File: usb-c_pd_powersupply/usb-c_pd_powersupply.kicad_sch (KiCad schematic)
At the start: 29 parts

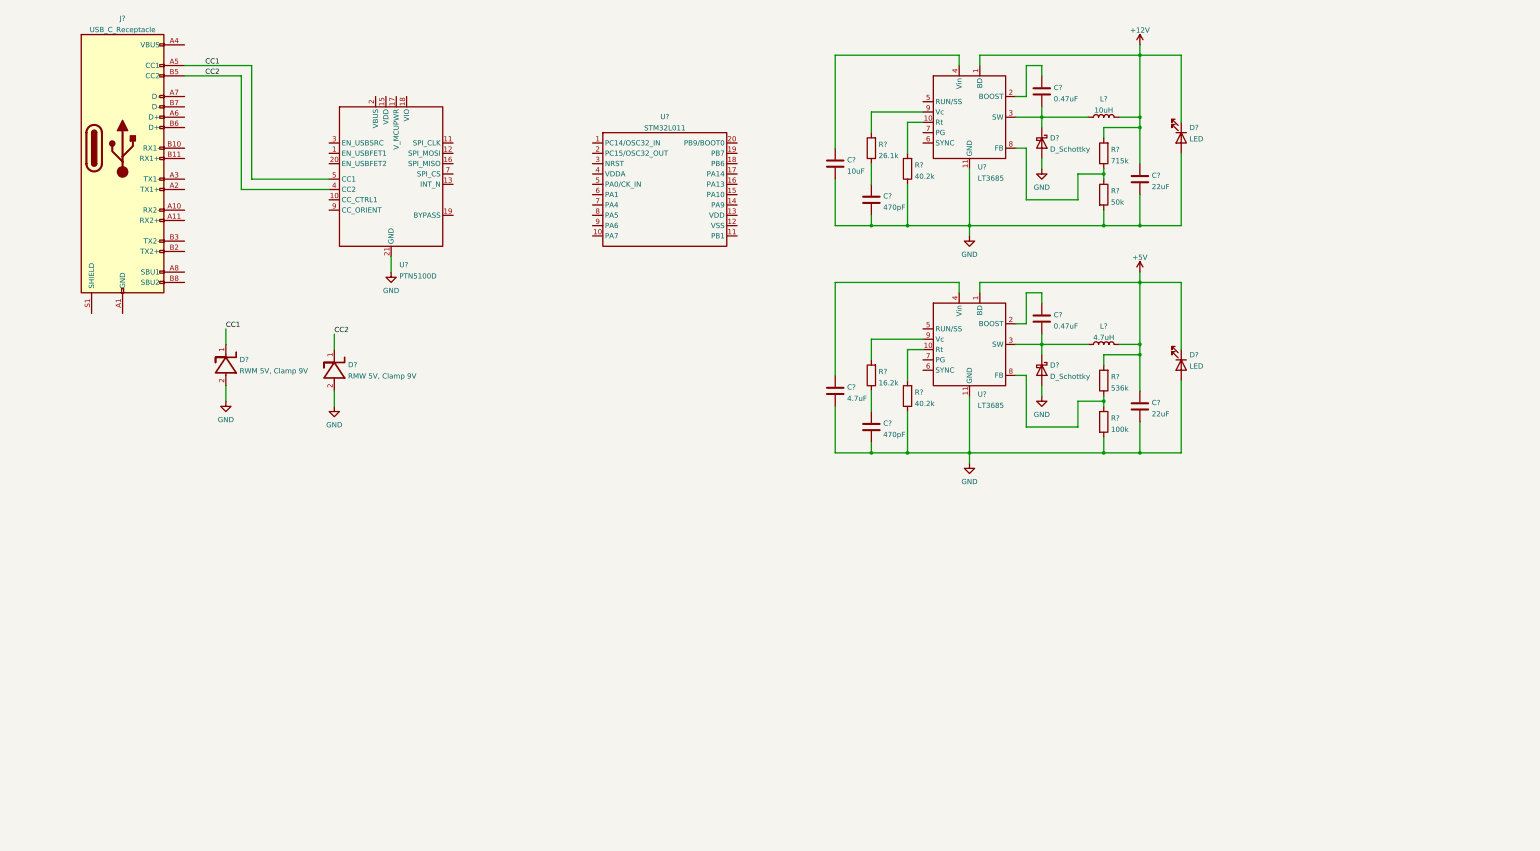
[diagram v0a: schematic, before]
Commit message: WIP on USB-C power supply
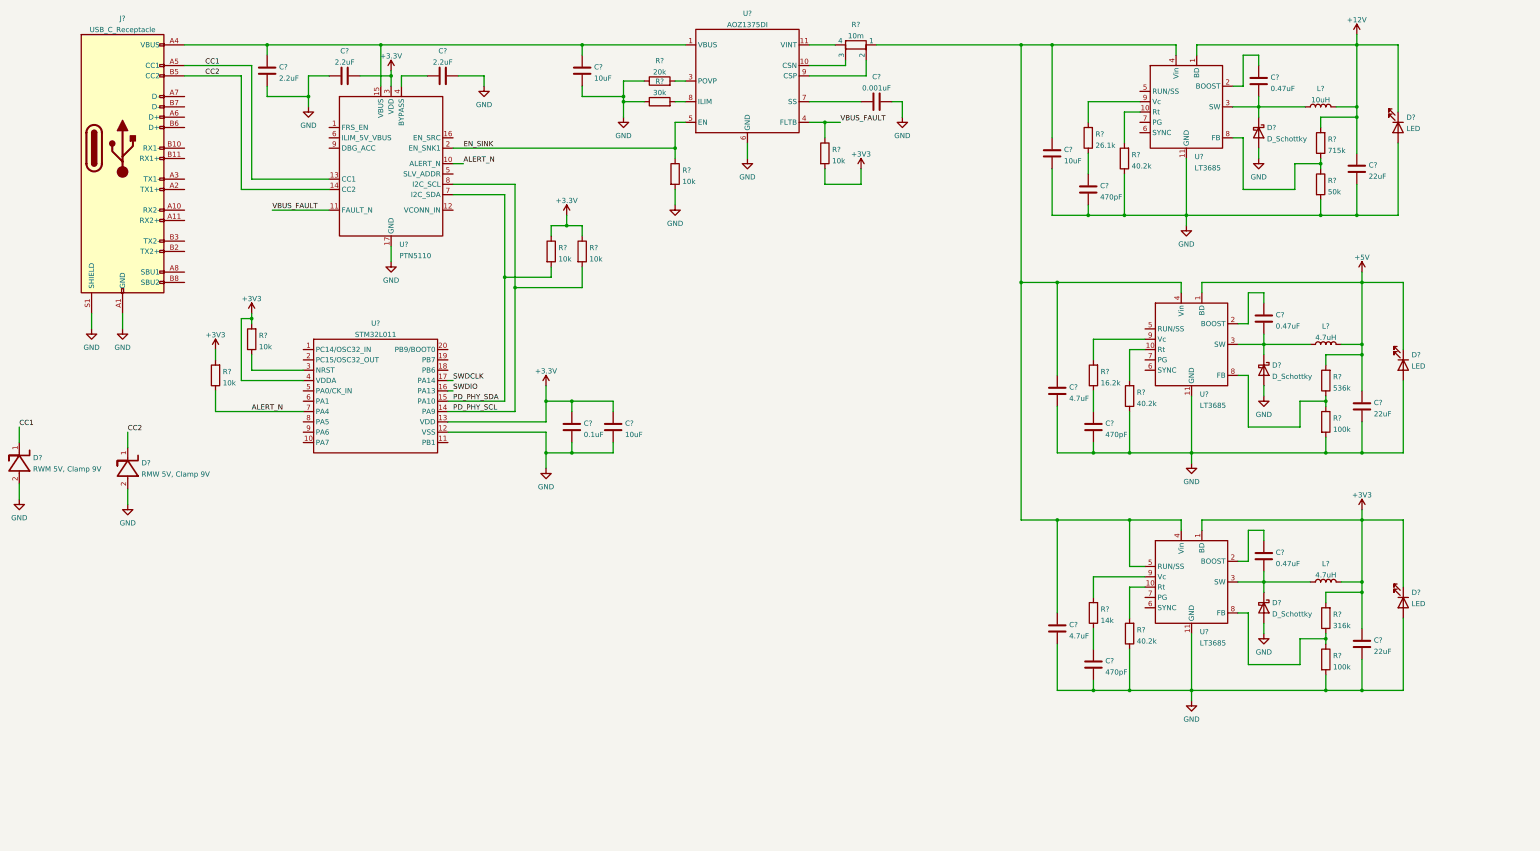
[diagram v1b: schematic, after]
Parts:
- removed U?: PTN5100D, Custom:HVQFN-20, symbol Custom:PTN5100D
- added C? (x2): 10uF, symbol Device:C
- added C?: 0.001uF, symbol Device:C
- added C?: 0.47uF, symbol Device:C
- added C?: 4.7uF, symbol Device:C
- added C?: 470pF, symbol Device:C
- added C? (x3): 2.2uF, symbol Device:C
- added C?: 22uF, symbol Device:C
- added C?: 0.1uF, symbol Device:C
- added D?: LED, symbol Device:LED
- added D?: D_Schottky, symbol Device:D_Schottky
- added L?: 4.7uH, symbol Device:L
- added R? (x6): 10k, symbol Device:R
- added R?: 10m, symbol Device:R_Shunt
- added R?: 14k, symbol Device:R
- added R?: 20k, symbol Device:R
- added R?: 30k, symbol Device:R
- added R?: 100k, symbol Device:R
- added R?: 316k, symbol Device:R
- added R?: 40.2k, symbol Device:R
- added U?: LT3685, Custom:DFN-10, symbol Custom:LT3685
- added U?: PTN5110, Custom:HX2QFN16, symbol Custom:PTN5110
- added U?: AOZ1375DI, Custom:DFN-12L, symbol Custom:AOZ1375DI
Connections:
- net CC1: now also U?.13 (CC1)
- net CC2: now also U?.14 (CC2)
- net GND: now also J?.A1 (GND), J?.A12 (GND), J?.B1 (GND), J?.B12 (GND), J?.S1 (SHIELD), U?.12 (VSS), C?.1, C?.1, C?.2, C?.2, C?.2, C?.2, C?.2, C?.2, C?.2, C?.2, D?.2 (A), D?.2 (A), R?.1, R?.1, R?.1, R?.2, R?.2, U?.11 (GND), U?.13 (GND), U?.17 (GND), U?.6 (GND)
- net at C?.1, U?.4 (Vin): now also C?.1, U?.4 (Vin), C?.1, R?.1, U?.4 (Vin), U?.5 (RUN/SS)
- net at J?.A4 (VBUS), J?.A9 (VBUS), J?.B4 (VBUS)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: now also C?.1, C?.2, U?.1 (VBUS), U?.15 (VBUS)
- net +3V3: now reaches U?.13 (VDD)
- net +3V3: now also U?.4 (VDDA), C?.1, C?.1, C?.1, C?.2, D?.1 (K), L?.2, R?.1, R?.1, R?.2, R?.2, R?.2, R?.2, U?.1 (BD), U?.3 (VDD)
- net PD_PHY_SCL: now reaches U?.14 (PA9)
- net PD_PHY_SCL: now also R?.2, U?.8 (I2C_SCL)
- net PD_PHY_SDA: now reaches U?.15 (PA10)
- net PD_PHY_SDA: now also R?.2, U?.7 (I2C_SDA)
- net SWDIO: now reaches U?.16 (PA13)
- net SWDCLK: now reaches U?.17 (PA14)
- net at U?.3 (NRST): now also R?.1
- net ALERT_N: now reaches U?.7 (PA4)
- net ALERT_N: now also R?.1, U?.10 (ALERT_N)
- new net: C?.1, U?.7 (SS)
- new net: C?.1, U?.2 (BOOST)
- new net: C?.2, D?.1 (K), L?.1, U?.3 (SW)
- new net: C?.1, R?.1
- new net: R?.2, U?.9 (CSP)
- new net: R?.3, U?.10 (CSN)
- new net: R?.4, U?.11 (VINT)
- new net: R?.2, U?.9 (Vc)
- new net: R?.2, U?.10 (Rt)
- new net: R?.1, R?.1, U?.8 (FB)
- new net: C?.1, U?.4 (BYPASS)
- new net: R?.2, U?.3 (POVP)
- new net: R?.2, U?.8 (ILIM)
- new net EN_SINK: R?.1, U?.2 (EN_SNK1), U?.5 (EN)
- new net VBUS_FAULT: R?.1, U?.11 (FAULT_N), U?.4 (FLTB)
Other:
- moved on the sheet: C?, D?, L?, R?, U?

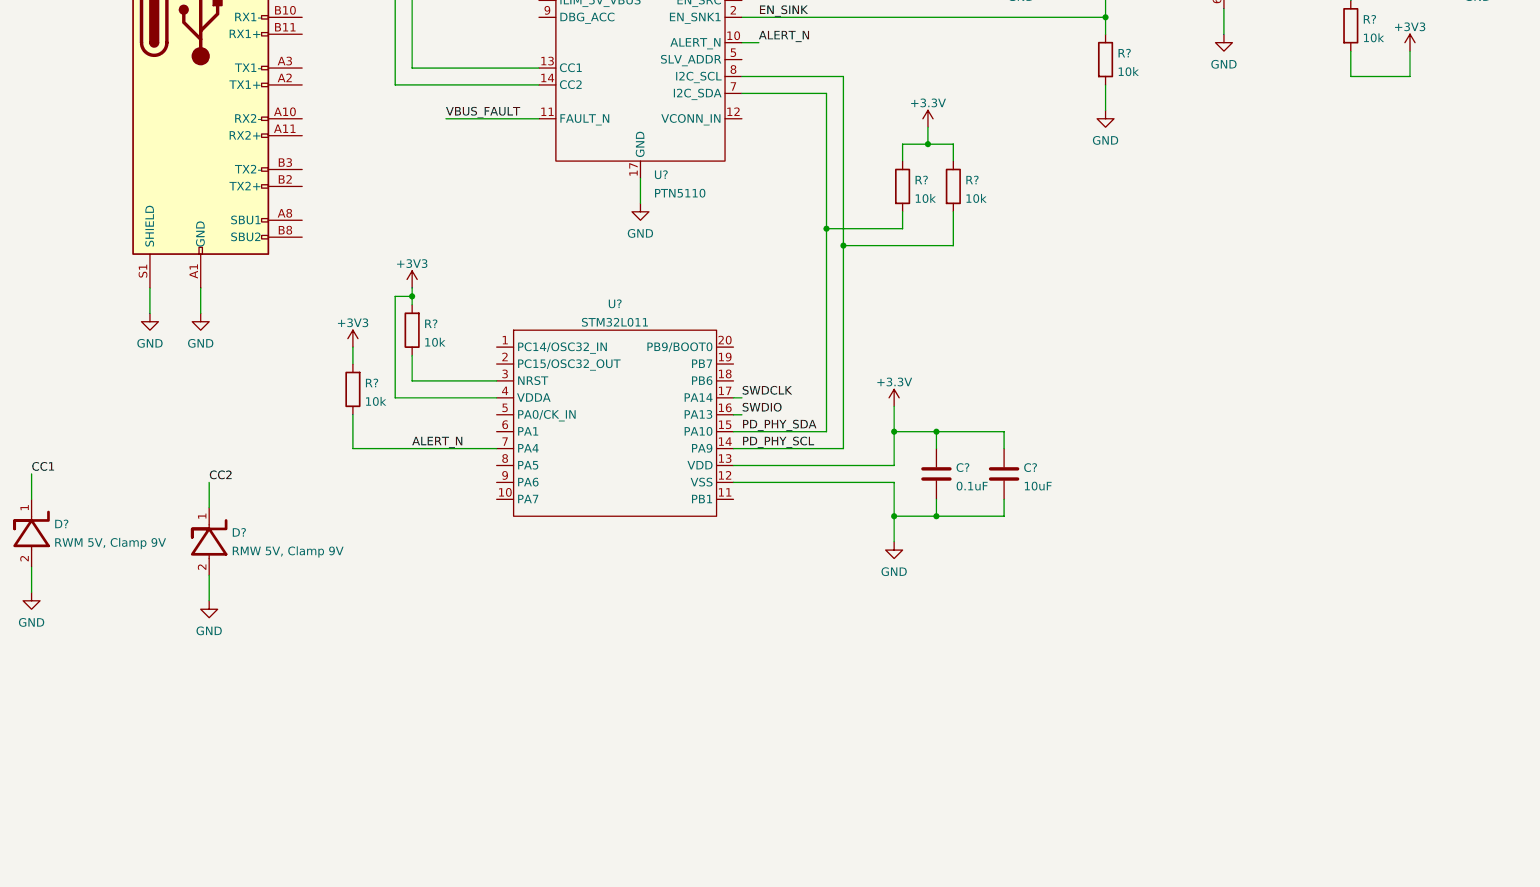
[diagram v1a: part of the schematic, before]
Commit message: Schematic first pass for pd supply
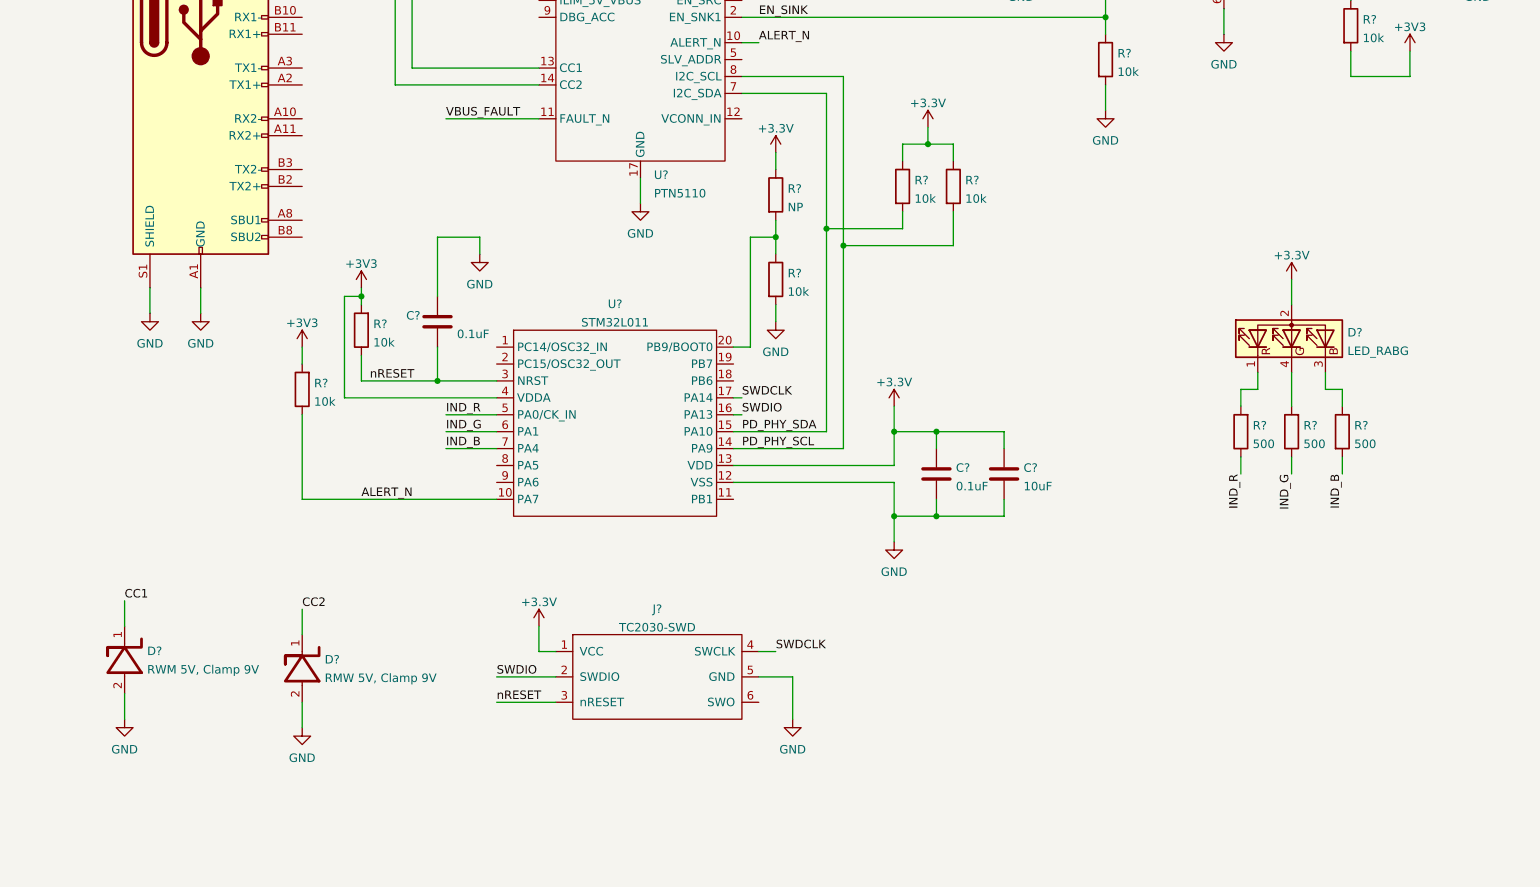
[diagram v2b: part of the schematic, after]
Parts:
- added C?: 0.1uF, symbol Device:C
- added D?: LED_RABG, symbol Device:LED_RABG
- added J?: TC2030-SWD, Custom:TC2030-IDC-FP, symbol Custom:TC2030-SWD
- added R? (x3): 500, symbol Device:R
- added R?: NP, symbol Device:R
- added R?: 10k, symbol Device:R
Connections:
- net +3V3: now also D?.2 (A), J?.1 (VCC), R?.1
- net ALERT_N: now also U?.10 (PA7); no longer U?.7 (PA4)
- net GND: now also C?.1, J?.5 (GND), R?.2
- net SWDCLK: now also J?.4 (SWCLK)
- net SWDIO: now also J?.2 (SWDIO)
- net nRESET: now reaches R?.1, U?.3 (NRST)
- net nRESET: now also C?.2, J?.3 (nRESET)
- net at U?.20 (PB9/BOOT0): now also R?.1, R?.2
- net IND_R: now reaches U?.5 (PA0/CK_IN)
- net IND_R: now also R?.1
- net IND_G: now reaches U?.6 (PA1)
- net IND_G: now also R?.1
- new net: D?.1 (RK), R?.2
- new net: D?.3 (BK), R?.1
- new net: D?.4 (GK), R?.2
- new net IND_B: R?.2, U?.7 (PA4)
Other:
- moved on the sheet: D?, R?

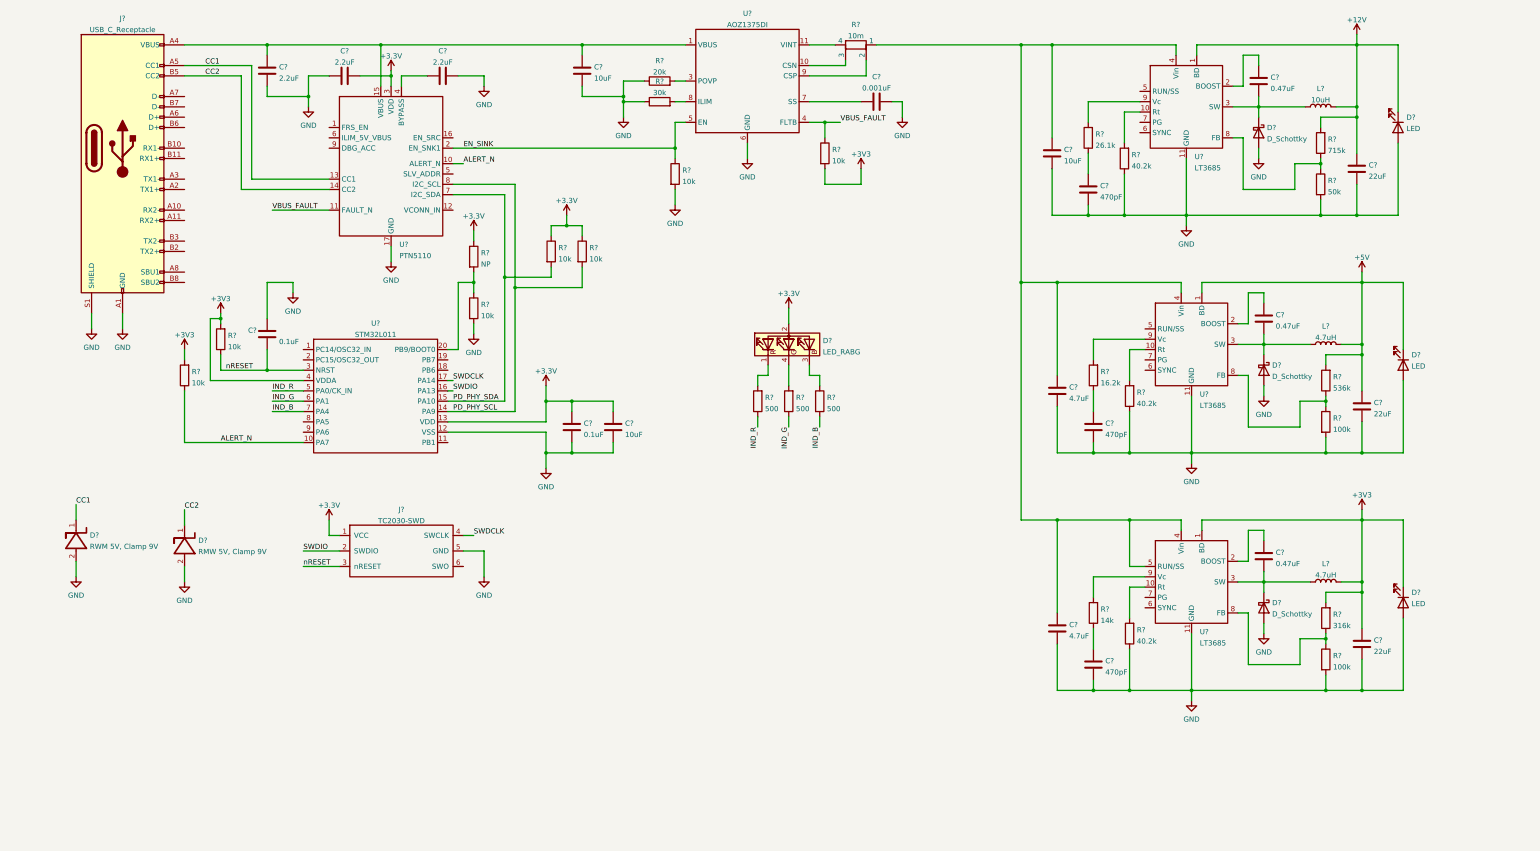
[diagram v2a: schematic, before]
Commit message: Progress on USB C Power Supply
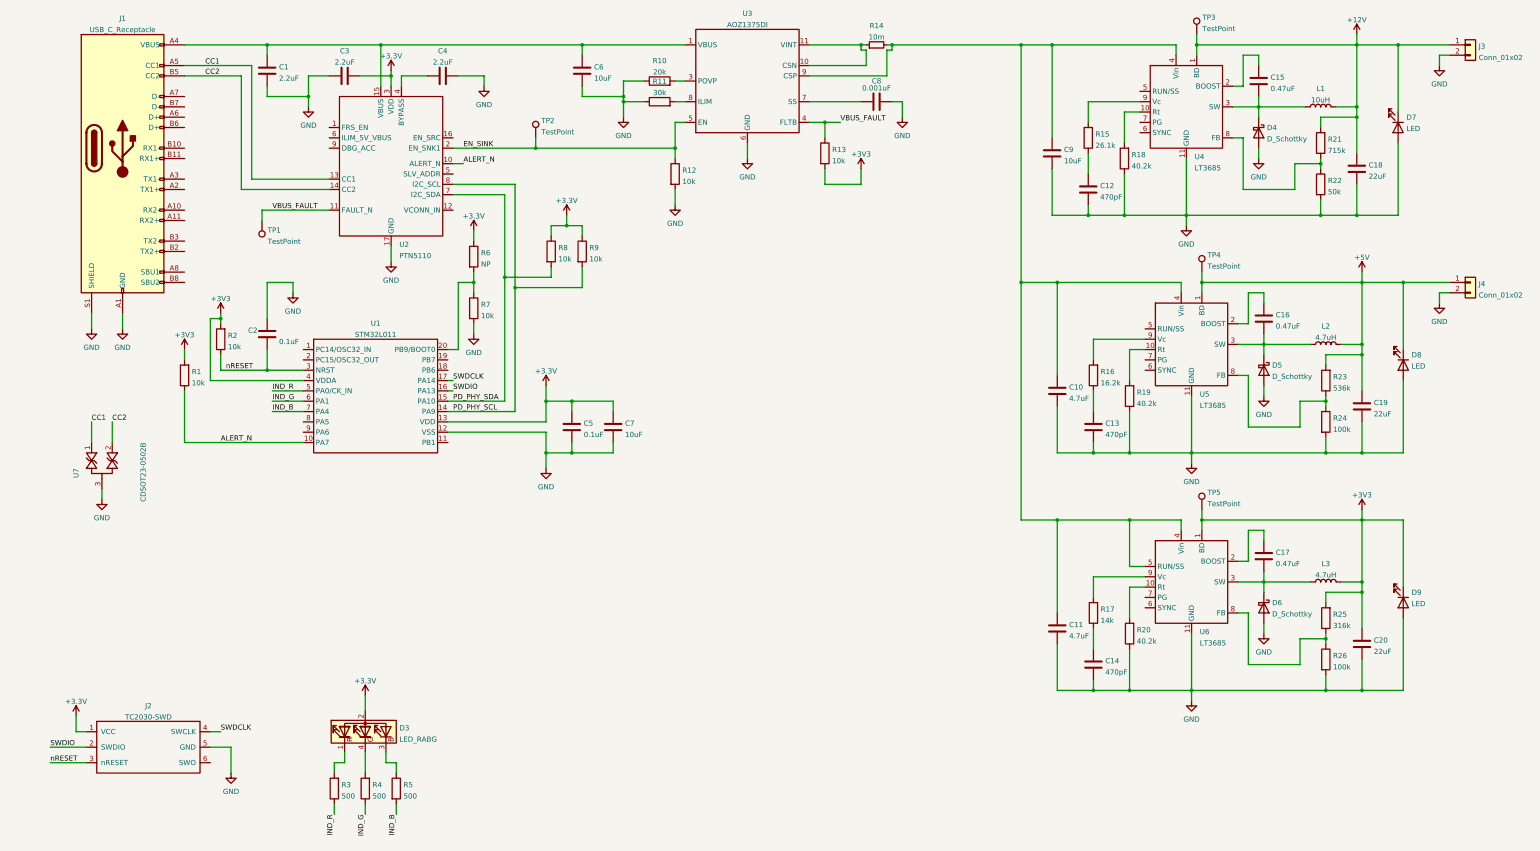
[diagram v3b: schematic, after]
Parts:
- removed D?: RMW 5V, Clamp 9V, symbol Custom:D_TVS
- removed D?: RWM 5V, Clamp 9V, symbol Custom:D_TVS
- removed R?: 10m, symbol Device:R_Shunt
- added J3, J4: Conn_01x02, Custom:PhoenixContact_1823638, symbol Connector_Generic:Conn_01x02
- added R14: 10m, Resistor_SMD:R_1206_3216Metric, symbol Device:R_Small
- added TP1, TP2, TP3, TP4, TP5: TestPoint, TestPoint:TestPoint_Pad_D2.0mm, symbol Connector:TestPoint
- added U7: CDSOT23-0502B, Custom:SOT23-3L, symbol Custom:CDSOT23-0502B
- C1, C10, C11, C12, C13, C14, C15, C16, C17, C18, C19, C2, C20, C3, C4, C5, C6, C7, C8, C9: renamed from C?; footprint (none) -> Capacitor_SMD:C_0805_2012Metric
- D3: renamed from D?; footprint (none) -> LED_SMD:LED_RGB_Wuerth-PLCC4_3.2x2.8mm_150141M173100
- D4, D5, D6: renamed from D?; footprint (none) -> Diode_SMD:D_SMB
- D7, D8, D9: renamed from D?; footprint (none) -> LED_SMD:LED_0805_2012Metric
- J1: renamed from J?; footprint (none) -> Custom:Wurth_632723300011
- L1, L2, L3: renamed from L?; footprint (none) -> Custom:SRP0620
- R1, R10, R11, R12, R13, R15, R16, R17, R18, R19, R2, R20, R21, R22, R23, R24, R25, R26, R3, R4, R5, R6, R7, R8, R9: renamed from R?; footprint (none) -> Resistor_SMD:R_0805_2012Metric
- gave numbers to parts that had none: 7
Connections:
- net +12V: now also J3.1 (Pin_1), TP3.1
- net +3V3: now also TP5.1
- net +5V: now also J4.1 (Pin_1), TP4.1
- net CC1: now also U7.1
- net CC2: now also U7.2
- net EN_SINK: now also TP2.1
- net GND: now also J3.2 (Pin_2), J4.2 (Pin_2), U7.3
- net VBUS_FAULT: now also TP1.1
- net at C10.1, C11.1, C9.1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: now also U3.9 (CSP), R14.2
- net at U3.10 (CSN): now also U3.11 (VINT), R14.1
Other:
- moved on the sheet: D3, J2, R3, R4, R5
